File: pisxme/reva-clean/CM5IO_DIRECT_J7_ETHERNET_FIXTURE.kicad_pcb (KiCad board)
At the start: 6 copper layers, 92 x 90 mm, 13 parts, among them J2 A70-112-331N126, J7 Raspberry-Pi-5-Compute-Module, U6 TPD4EUSB30, U9 TPD4EUSB30

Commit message: phase17: refine colocated ethernet support witness
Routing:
- net ETH_CT3: track 15.6 -> 30.1 mm
- net ETH_CT2: track 16.8 -> 26.0 mm

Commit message: phase17: close disposable ethernet support crossings
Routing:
- net ETH_CT4: vias 0 -> 2

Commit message: phase17: close ethernet routing gate
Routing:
- net ETH_GND: vias 7 -> 6
- net ETH_CT4: vias 2 -> 1

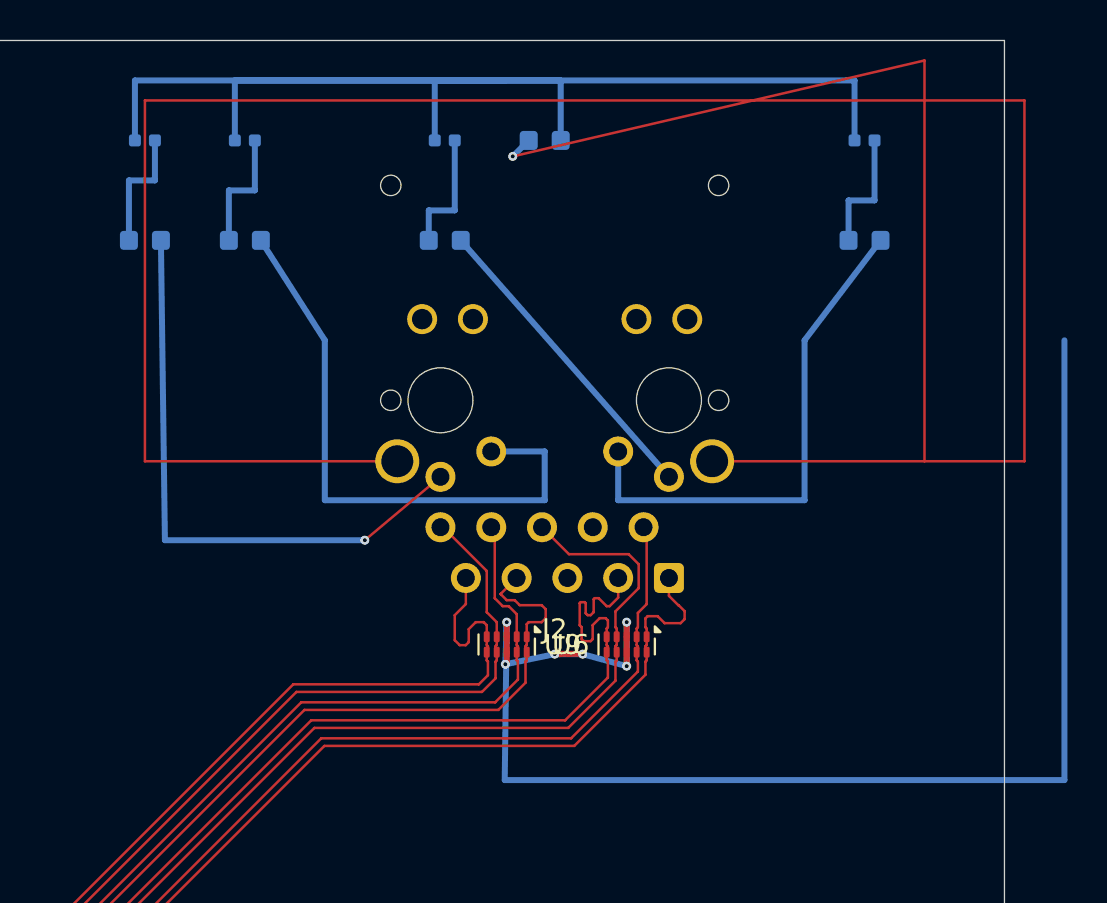
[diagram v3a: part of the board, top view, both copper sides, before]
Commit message: phase24: preserve official Ethernet transplant oracle
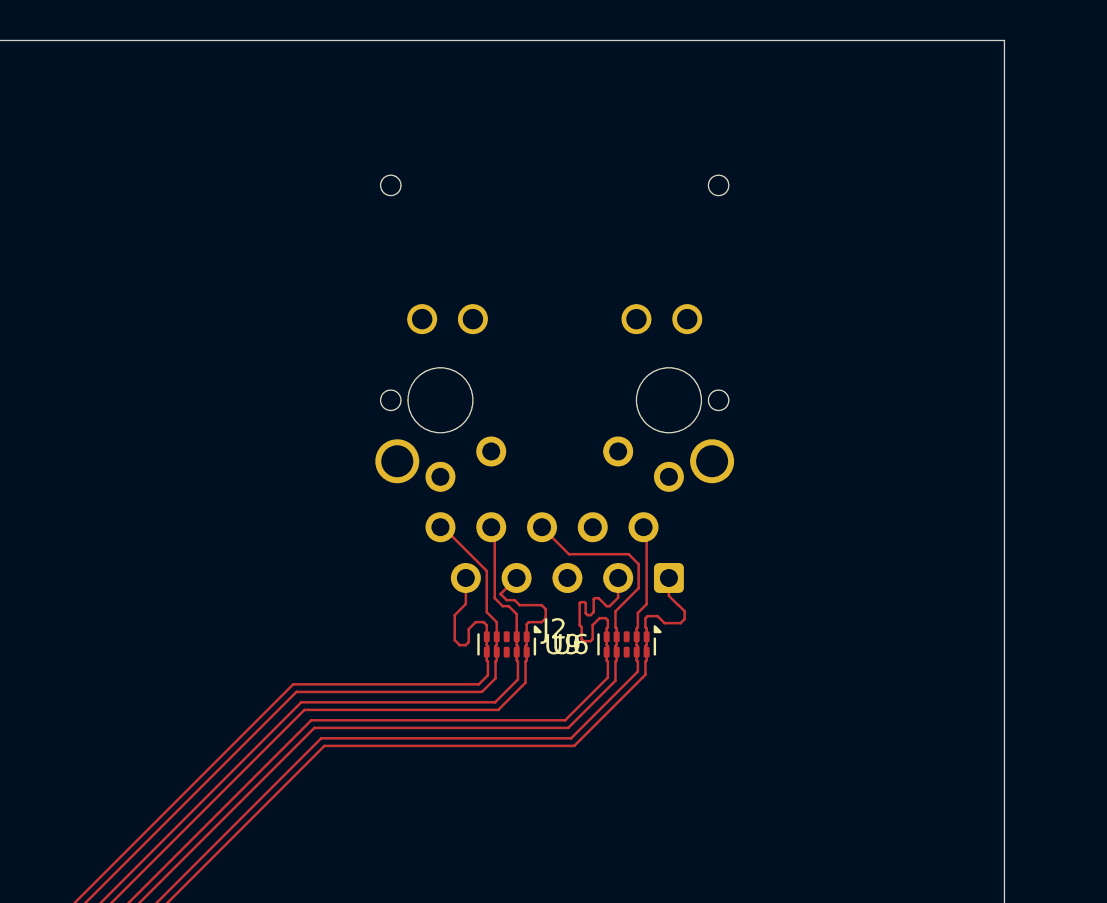
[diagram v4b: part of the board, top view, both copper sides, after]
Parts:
- removed CCT, CCT1, CCT2, CCT3, CCT4: C_0603_1608Metric, C_0603_1608Metric
- removed RCT1, RCT2, RCT3, RCT4: R_0402_1005Metric, R_0402_1005Metric
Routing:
- net GBE_SHIELD: track 150.7 -> 0.00 mm, vias 1 -> 0
- net ETH_GND: track 74.2 -> 0.00 mm, vias 6 -> 0
- net ETH_CT_COMMON: track 70.8 -> 0.00 mm
- net ETH_CT3: track 30.1 -> 0.00 mm
- net ETH_CT4: track 29.9 -> 0.00 mm, vias 1 -> 0
- net ETH_CT2: track 26.0 -> 0.00 mm
- net ETH_CT1: track 15.8 -> 0.00 mm
- net ETH_CT_BRANCH_4: track 6.30 -> 0.00 mm
- net ETH_CT_BRANCH_3: track 6.30 -> 0.00 mm
- net ETH_CT_BRANCH_2: track 6.30 -> 0.00 mm
- net ETH_CT_BRANCH_1: track 6.30 -> 0.00 mm

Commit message: phase24: close complete CM5IO Ethernet fixture oracle
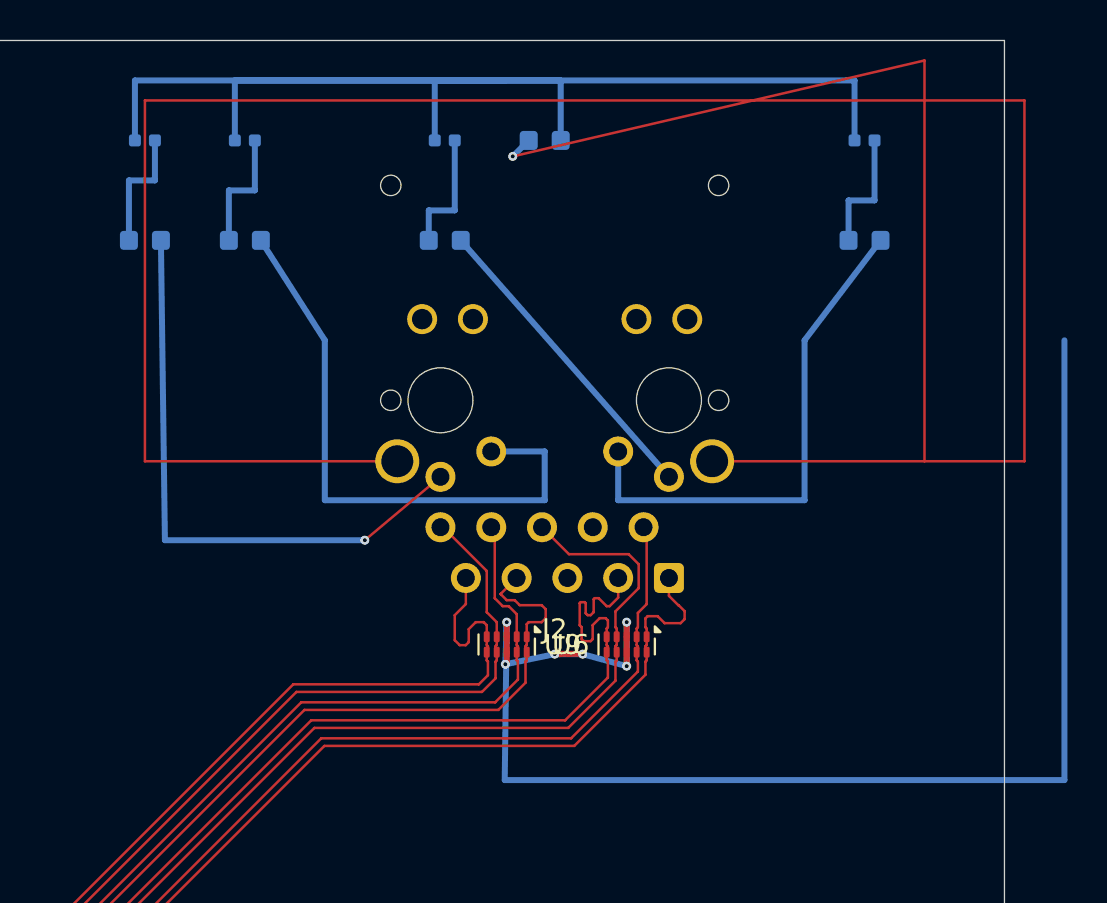
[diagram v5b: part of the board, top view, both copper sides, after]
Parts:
- added CCT: C_0603_1608Metric, C_0603_1608Metric, B.Cu at (77.0, 40.0)
- added CCT1: C_0603_1608Metric, C_0603_1608Metric, B.Cu at (72.0, 45.0)
- added CCT2: C_0603_1608Metric, C_0603_1608Metric, B.Cu at (93.0, 45.0)
- added CCT3: C_0603_1608Metric, C_0603_1608Metric, B.Cu at (62.0, 45.0)
- added CCT4: C_0603_1608Metric, C_0603_1608Metric, B.Cu at (57.0, 45.0)
- added RCT1: R_0402_1005Metric, R_0402_1005Metric, B.Cu at (72.0, 40.0)
- added RCT2: R_0402_1005Metric, R_0402_1005Metric, B.Cu at (93.0, 40.0)
- added RCT3: R_0402_1005Metric, R_0402_1005Metric, B.Cu at (62.0, 40.0)
- added RCT4: R_0402_1005Metric, R_0402_1005Metric, B.Cu at (57.0, 40.0)
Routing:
- net GBE_SHIELD: track 0.00 -> 150.7 mm, vias 0 -> 1
- net ETH_GND: track 0.00 -> 74.2 mm, vias 0 -> 6
- net ETH_CT_COMMON: track 0.00 -> 70.8 mm
- net ETH_CT3: track 0.00 -> 30.1 mm
- net ETH_CT4: track 0.00 -> 29.9 mm, vias 0 -> 1
- net ETH_CT2: track 0.00 -> 26.0 mm
- net ETH_CT1: track 0.00 -> 15.8 mm
- net ETH_CT_BRANCH_4: track 0.00 -> 6.30 mm
- net ETH_CT_BRANCH_3: track 0.00 -> 6.30 mm
- net ETH_CT_BRANCH_2: track 0.00 -> 6.30 mm
- net ETH_CT_BRANCH_1: track 0.00 -> 6.30 mm
